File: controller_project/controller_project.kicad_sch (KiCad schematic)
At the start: 16 parts, among them U5 COM-09032, U6 COM-09032

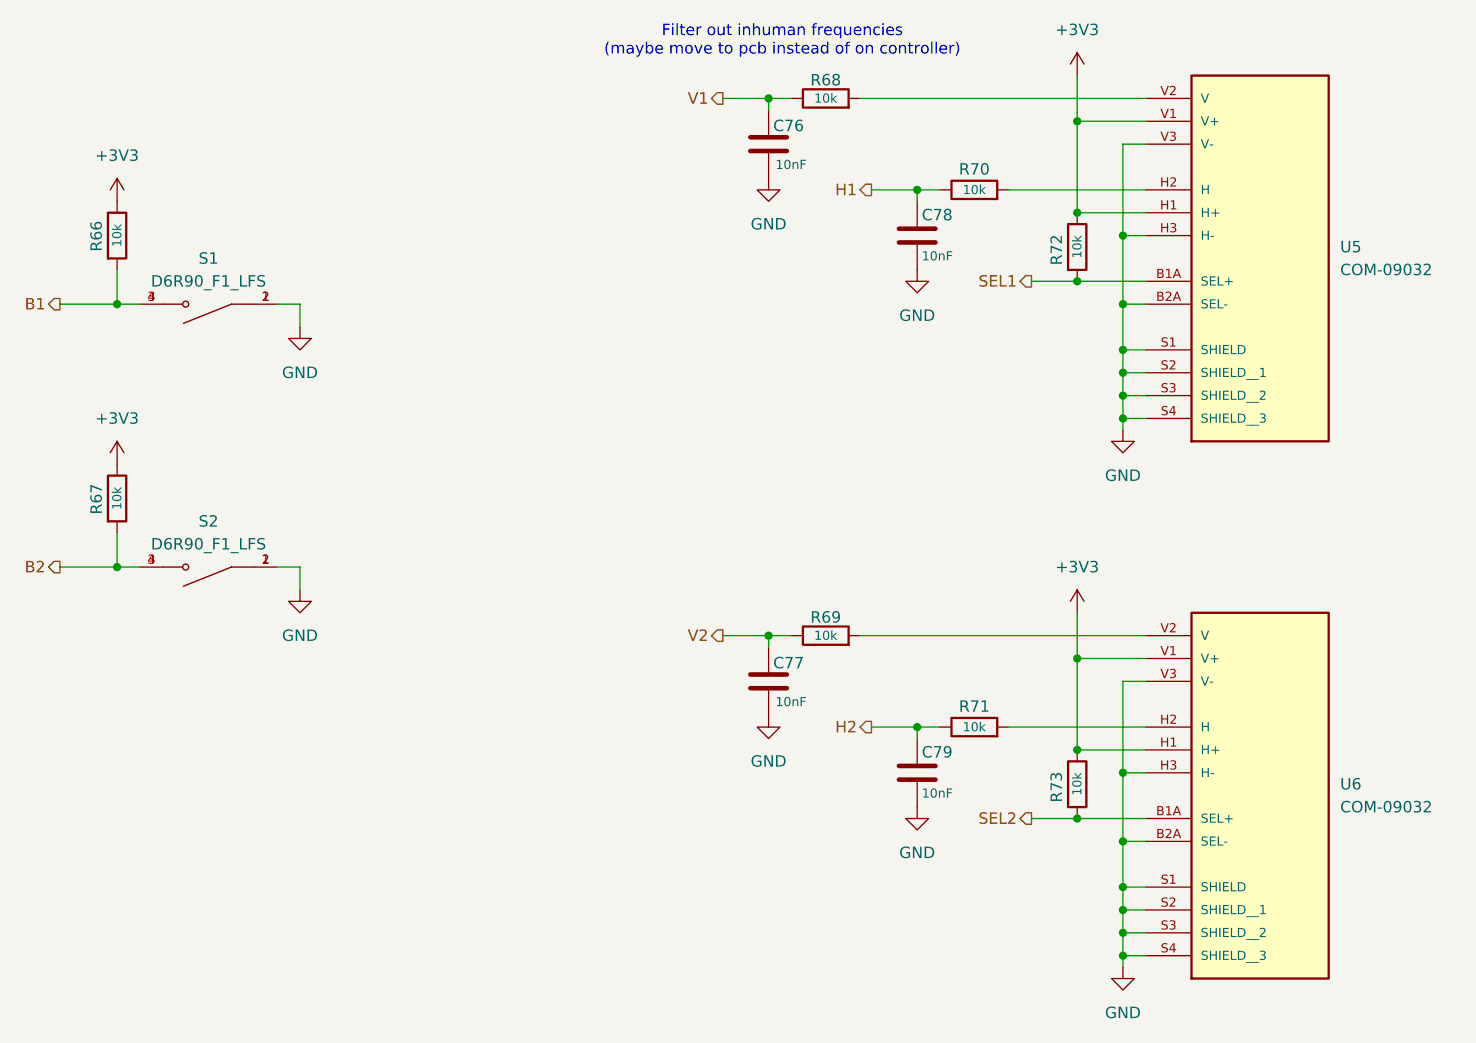
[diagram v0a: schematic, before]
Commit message: Update controller connector schematic
- Fix pin component so it works in layout
- Move RC filters from controller to PCB
- Remove pullups from controller as they are on pcb
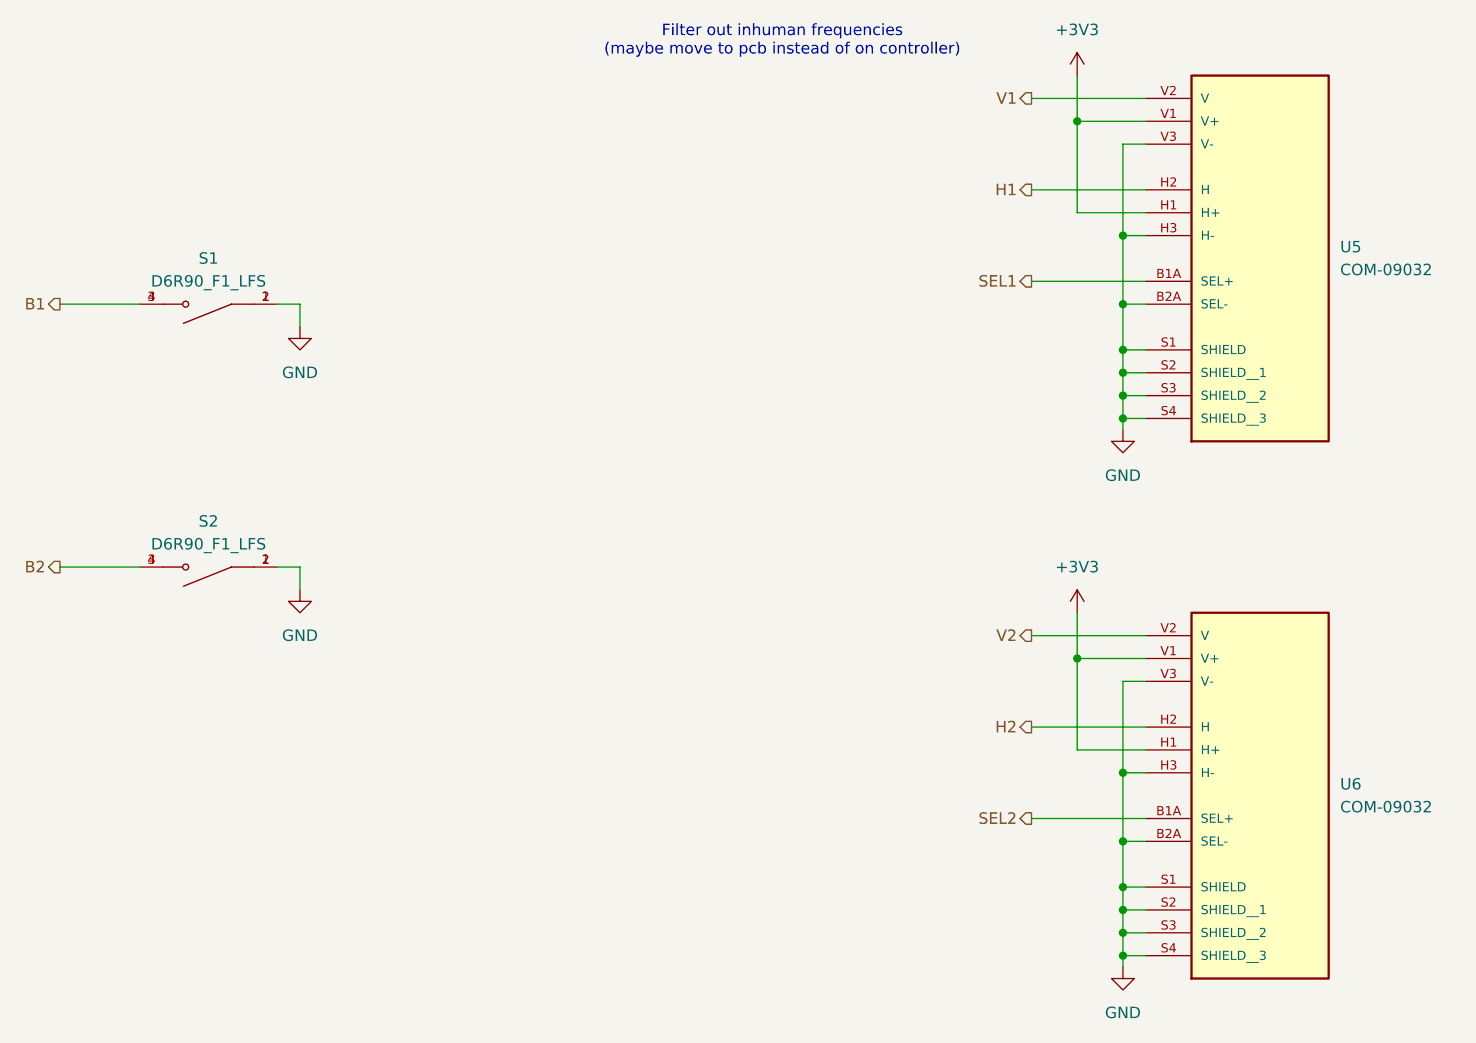
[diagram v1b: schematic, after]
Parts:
- removed C76, C77, C78, C79: 10nF, Capacitor_SMD:C_0603_1608Metric_Pad1.08x0.95mm_HandSolder, symbol Device:C
- removed R66, R67, R68, R69, R70, R71, R72, R73: 10k, Resistor_SMD:R_0805_2012Metric_Pad1.20x1.40mm_HandSolder, symbol Device:R
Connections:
- net H1: now also U5.H2 (H)
- net H2: now also U6.H2 (H)
- net V1: now also U5.V2 (V)
- net V2: now also U6.V2 (V)
